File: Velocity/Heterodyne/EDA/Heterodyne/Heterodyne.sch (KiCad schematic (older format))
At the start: 37 parts, among them J1 Conn_01x05, J7 Reciever, U1 SA612AD, U2 NE5532DR, U3 MAX7375AXR105, U4 MAX11613, U5 ATmega328PB-AU, Y1 8 MHz

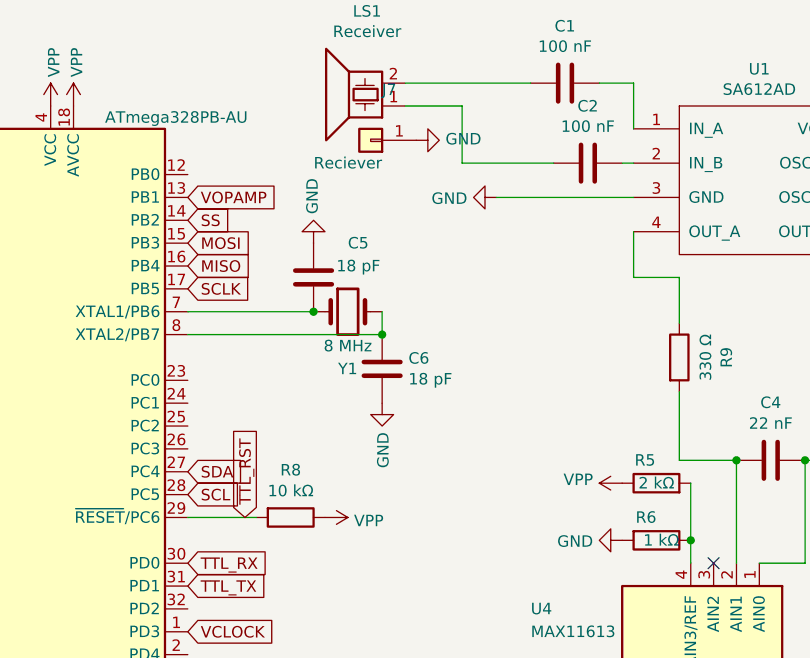
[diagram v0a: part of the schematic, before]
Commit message: Velocity: changed supply for ADC ref voltage devider from VPP to arduino pin, est current saveings 1 mA
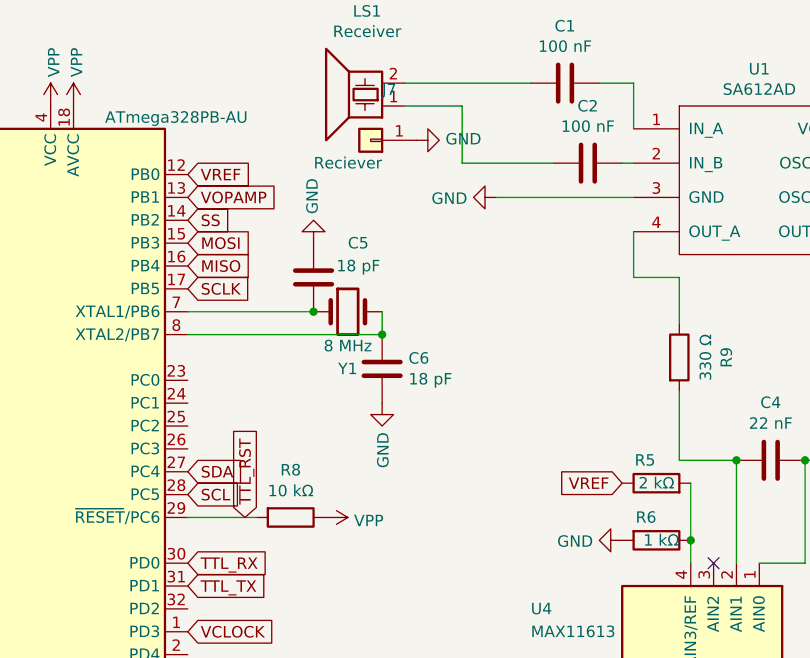
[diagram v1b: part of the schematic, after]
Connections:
- net VPP: no longer R5.1
- net VREF: now reaches U5.12 (PB0)
- net VREF: now also R5.1
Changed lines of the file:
@@
 	5000 4150 5000 4050
-$Comp
-L Heterodyne-rescue:VPP-power #PWR0103
-U 1 1 5E43C439
-P 4700 3800
-F 0 "#PWR0103" H 4700 3650 50  0001 C CNN
-F 1 "VPP" V 4715 3927 50  0000 L CNN
-F 2 "" H 4700 3800 50  0001 C CNN
-F 3 "" H 4700 3800 50  0001 C CNN
-	1    4700 3800
-	0    -1   -1   0
-$EndComp
 $Comp
 L Heterodyne-rescue:GND-power #PWR0104
@@
 $EndComp
 NoConn ~ 1600 2450
+Text GLabel 2800 2450 2    50   Input ~ 0
+VREF
+Text GLabel 4700 3800 0    50   Input ~ 0
+VREF
 $EndSCHEMATC

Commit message: finished bosl board rev0.4 layout
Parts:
- removed J1: Conn_01x05, Connector_PinHeader_2.54mm:PinHeader_1x05_P2.54mm_Vertical, symbol Connector_Generic:Conn_01x05
- added C7: 100 nF, Capacitor_SMD:C_0603_1608Metric_Pad1.05x0.95mm_HandSolder, symbol Heterodyne-rescue:C-Device
- added J1: Conn_01x06, Connector_PinHeader_2.54mm:PinHeader_1x06_P2.54mm_Vertical, symbol Connector_Generic:Conn_01x06
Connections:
- net GND: now also C7.2, J1.2 (Pin_2)
- net TTL_RST: now also J1.3 (Pin_3)
- net TTL_RX: now also J1.4 (Pin_4)
- net TTL_TX: now also J1.5 (Pin_5)
- net VPP: now also J1.1 (Pin_1)
- net VREF: now also U5.23 (PC0); no longer U5.12 (PB0)
- net at R5.2, R6.1, U4.4 (AIN3/REF): now also C7.1
- net TLL_WAKE: now reaches U5.32 (PD2)
- net TLL_WAKE: now also J1.6 (Pin_6)
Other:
- moved on the sheet: R5
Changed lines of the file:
@@
 L Heterodyne-rescue:GND-power #PWR0123
 U 1 1 5E3B45F2
-P 8450 4950
-F 0 "#PWR0123" H 8450 4700 50  0001 C CNN
-F 1 "GND" V 8455 4823 50  0000 R CNN
-F 2 "" H 8450 4950 50  0001 C CNN
-F 3 "" H 8450 4950 50  0001 C CNN
-	1    8450 4950
+P 8600 4950
+F 0 "#PWR0123" H 8600 4700 50  0001 C CNN
+F 1 "GND" V 8605 4823 50  0000 R CNN
+F 2 "" H 8600 4950 50  0001 C CNN
+F 3 "" H 8600 4950 50  0001 C CNN
+	1    8600 4950
 	-1   0    0    1
 $EndComp
@@
 L Heterodyne-rescue:VPP-power #PWR0124
 U 1 1 5E3B49BA
-P 8550 4950
-F 0 "#PWR0124" H 8550 4800 50  0001 C CNN
-F 1 "VPP" V 8565 5076 50  0000 L CNN
-F 2 "" H 8550 4950 50  0001 C CNN
-F 3 "" H 8550 4950 50  0001 C CNN
-	1    8550 4950
+P 8700 4950
+F 0 "#PWR0124" H 8700 4800 50  0001 C CNN
+F 1 "VPP" V 8715 5076 50  0000 L CNN
+F 2 "" H 8700 4950 50  0001 C CNN
+F 3 "" H 8700 4950 50  0001 C CNN
+	1    8700 4950
 	1    0    0    -1
 $EndComp
@@
 U 1 1 5E436A94
 P 4850 4050
-F 0 "R6" V 4750 4050 50  0000 R CNN
+F 0 "R6" V 4950 4050 50  0000 R CNN
 F 1 "1 kΩ" V 4850 4150 50  0000 R CNN
 F 2 "Resistor_SMD:R_0603_1608Metric_Pad1.05x0.95mm_HandSolder" V 4780 4050 50  0001 C CNN
@@
 L Device:R R5
 U 1 1 5E436F78
-P 4850 3800
-F 0 "R5" V 4950 3850 50  0000 C CNN
-F 1 "2 kΩ" V 4850 3800 50  0000 C CNN
-F 2 "Resistor_SMD:R_0603_1608Metric_Pad1.05x0.95mm_HandSolder" V 4780 3800 50  0001 C CNN
-F 3 "~" H 4850 3800 50  0001 C CNN
-	1    4850 3800
+P 4750 3550
+F 0 "R5" V 4850 3600 50  0000 C CNN
+F 1 "2 kΩ" V 4750 3550 50  0000 C CNN
+F 2 "Resistor_SMD:R_0603_1608Metric_Pad1.05x0.95mm_HandSolder" V 4680 3550 50  0001 C CNN
+F 3 "~" H 4750 3550 50  0001 C CNN
+	1    4750 3550
 	0    -1   -1   0
 $EndComp
@@
 Wire Wire Line
 	5650 3700 5500 3700
-Wire Wire Line
-	5000 3800 5000 4050
-Connection ~ 5000 4050
 Wire Wire Line
 	5200 4150 5200 3700
@@
 	1    4600 5200
 	0    -1   -1   0
-$EndComp
-$Comp
-L MCU_Microchip_ATmega:ATmega328PB-AU U5
-U 1 1 5E452B6B
-P 2200 3650
-F 0 "U5" H 1750 5150 50  0000 C CNN
-F 1 "ATmega328PB-AU" H 2750 5100 50  0000 C CNN
-F 2 "Package_QFP:TQFP-32_7x7mm_P0.8mm" H 2200 3650 50  0001 C CIN
-F 3 "http://ww1.microchip.com/downloads/en/DeviceDoc/40001906C.pdf" H 2200 3650 50  0001 C CNN
-	1    2200 3650
-	1    0    0    -1
 $EndComp
 $Comp
@@
 Text GLabel 3050 3950 1    50   Input ~ 0
 TTL_RST
-Text GLabel 8350 4950 1    50   Input ~ 0
+Text GLabel 8500 4950 1    50   Input ~ 0
 TTL_RST
-Text GLabel 8250 4950 1    50   Input ~ 0
+Text GLabel 8400 4950 1    50   Input ~ 0
 TTL_RX
-Text GLabel 8150 4950 1    50   Input ~ 0
+Text GLabel 8300 4950 1    50   Input ~ 0
 TTL_TX
 $Comp
@@
 Text GLabel 7000 3400 1    50   Input ~ 0
 VOPAMP
-$Comp
-L Connector_Generic:Conn_01x05 J1
-U 1 1 5E4B4FBE
-P 8350 5150
-F 0 "J1" V 8222 5430 50  0000 L CNN
-F 1 "Conn_01x05" V 8313 5430 50  0000 L CNN
-F 2 "Connector_PinHeader_2.54mm:PinHeader_1x05_P2.54mm_Vertical" H 8350 5150 50  0001 C CNN
-F 3 "~" H 8350 5150 50  0001 C CNN
-	1    8350 5150
-	0    1    1    0
-$EndComp
 Text Notes 2350 1450 0    50   ~ 0
 OPTIMISATION IDEA: USE ARDUINO TO GENERATE 1MHz WAVE
@@
 $EndComp
 NoConn ~ 1600 2450
-Text GLabel 2800 2450 2    50   Input ~ 0
+Text GLabel 2800 3350 2    50   Input ~ 0
 VREF
-Text GLabel 4700 3800 0    50   Input ~ 0
+Text GLabel 4600 3550 0    50   Input ~ 0
 VREF
+$Comp
+L Connector_Generic:Conn_01x06 J1
+U 1 1 5E9822C7
+P 8500 5150
+F 0 "J1" V 8372 5430 50  0000 L CNN
+F 1 "Conn_01x06" V 8463 5430 50  0000 L CNN
+F 2 "Connector_PinHeader_2.54mm:PinHeader_1x06_P2.54mm_Vertical" H 8500 5150 50  0001 C CNN
+F 3 "~" H 8500 5150 50  0001 C CNN
+	1    8500 5150
+	0    1    1    0
+$EndComp
+Text GLabel 2800 4350 2    50   Input ~ 0
+TLL_WAKE
+$Comp
+L MCU_Microchip_ATmega:ATmega328PB-AU U5
+U 1 1 5E452B6B
+P 2200 3650
+F 0 "U5" H 1750 5150 50  0000 C CNN
+F 1 "ATmega328PB-AU" H 2750 5100 50  0000 C CNN
+F 2 "Package_QFP:TQFP-32_7x7mm_P0.8mm" H 2200 3650 50  0001 C CIN
+F 3 "http://ww1.microchip.com/downloads/en/DeviceDoc/40001906C.pdf" H 2200 3650 50  0001 C CNN
+	1    2200 3650
+	1    0    0    -1
+$EndComp
+Text GLabel 8200 4950 1    50   Input ~ 0
+TLL_WAKE
+$Comp
+L Heterodyne-rescue:C-Device C7
+U 1 1 5E989C6F
+P 4850 3900
+F 0 "C7" V 4600 3850 50  0000 C CNN
+F 1 "100 nF" V 4700 3800 50  0000 C CNN
+F 2 "Capacitor_SMD:C_0603_1608Metric_Pad1.05x0.95mm_HandSolder" H 4888 3750 50  0001 C CNN
+F 3 "~" H 4850 3900 50  0001 C CNN
+	1    4850 3900
+	0    1    1    0
+$EndComp
+$Comp
+L Heterodyne-rescue:GND-power #PWR01
+U 1 1 5E9905FE
+P 4700 3900
+F 0 "#PWR01" H 4700 3650 50  0001 C CNN
+F 1 "GND" V 4705 3773 50  0000 R CNN
+F 2 "" H 4700 3900 50  0001 C CNN
+F 3 "" H 4700 3900 50  0001 C CNN
+	1    4700 3900
+	0    1    1    0
+$EndComp
+Wire Wire Line
+	5000 4050 5000 3900
+Connection ~ 5000 4050
+Wire Wire Line
+	4900 3750 5000 3750
+Wire Wire Line
+	5000 3750 5000 3900
+Connection ~ 5000 3900
+Wire Wire Line
+	4900 3550 4900 3750
 $EndSCHEMATC
